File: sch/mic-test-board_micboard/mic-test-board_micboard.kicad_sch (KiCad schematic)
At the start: 25 parts, among them J1 Conn_01x01, J2 Conn_01x01, J3 Conn_01x01, J4 Conn_01x01, J5 Conn_01x01, J6 Conn_01x04, U1 ICS-40730, U2 THS4531AIRUNR

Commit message: pcb: finished routing mic board and ADC board.
 - BOM complete
 - uController pinout configured with CubeMX and re-checked
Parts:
- C6, C7: Manufacturer (none) -> Würth Elektronik; Part Number (none) -> 885012006027; Supplier (none) -> Digi-Key; Supplier Number (none) -> 732-7770-1-ND
- J1, J2, J3, J4, J5: now not fitted
- J6: value Conn_01x04 -> Conn_01x05; Manufacturer (none) -> Molex; Part Number (none) -> 0530470510; Supplier (none) -> Digi-Key; Supplier Number (none) -> WM1734-ND
- R1, R2: value 550R -> 549R; Manufacturer (none) -> YAGEO; Part Number (none) -> RC0603FR-07549RL; Supplier (none) -> Digi-Key; Supplier Number (none) -> 311-549HRCT-ND
- R3, R4: value 1.6k -> 1.58k; Manufacturer (none) -> YAGEO; Part Number (none) -> RC0603FR-071K58L; Supplier (none) -> Digi-Key; Supplier Number (none) -> 311-1.58KHRCT-ND
- U1: Manufacturer (none) -> TDK InvenSense; Part Number (none) -> ICS-40730; Supplier (none) -> Digi-Key; Supplier Number (none) -> 1428-1141-1-ND

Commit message: pcb: ordered PCB's and BOM! RevA and v240506
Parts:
- C1, C4: now in the parts list
- C11, C8: Manufacturer KEMET -> Samsung Electro-Mechanics; Part Number C0603C104K8RAC7867 -> CL10B105KP8NNNC; Supplier Number 399-C0603C104K8RAC7867CT-ND -> 1276-1946-1-ND
- J1, J2, J3, J4, J5: now fitted; now left out of the parts list
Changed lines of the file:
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@@
 		(unit 1)
 		(exclude_from_sim no)
-		(in_bom yes)
+		(in_bom no)
 		(on_board yes)
-		(dnp yes)
+		(dnp no)
 		(property "Reference" "J4"
 			(at 340.36 125.222 90)
@@
 	)
 	(symbol
+		(lib_name "THS4531AIRUNR_1")
 		(lib_id "mic-test-pcb:THS4531AIRUNR")
 		(at 231.14 146.05 0)
@@
 			)
 		)
-		(property "Description" "IC OPAMP DIFF 1 CIRCUIT 10WQFN"
+		(property "Description" "Ultralow Power, Low Distortion, Fully Differential ADC Drivers, Dual-Channel, "
 			(at 235.966 131.318 0)
 			(effects
@@
 		)
 		(pin "1"
+		)
+		(pin "8"
+		)
+		(pin "2"
 		)
 		(instances
@@
 			)
 		)
-		(property "Description" "IC OPAMP DIFF 1 CIRCUIT 10WQFN"
+		(property "Description" "Ultralow Power, Low Distortion, Fully Differential ADC Drivers, Dual-Channel, "
 			(at 221.996 227.838 0)
 			(effects
@@
 		(unit 1)
 		(exclude_from_sim no)
-		(in_bom yes)
+		(in_bom no)
 		(on_board yes)
-		(dnp yes)
+		(dnp no)
 		(property "Reference" "J2"
 			(at 332.74 125.222 90)
@@
 		(unit 1)
 		(exclude_from_sim no)
-		(in_bom yes)
+		(in_bom no)
 		(on_board yes)
-		(dnp yes)
+		(dnp no)
 		(property "Reference" "J1"
 			(at 328.93 125.222 90)
@@
 			)
 		)
-		(property "Manufacturer" "KEMET"
+		(property "Manufacturer" "Samsung Electro-Mechanics"
 			(at 254 243.84 0)
 			(effects
@@
 			)
 		)
-		(property "Part Number" "C0603C104K8RAC7867"
+		(property "Part Number" "CL10B105KP8NNNC"
 			(at 254 243.84 0)
 			(effects
@@
 			)
 		)
-		(property "Supplier Number" "399-C0603C104K8RAC7867CT-ND"
+		(property "Supplier Number" "1276-1946-1-ND"
 			(at 254 243.84 0)
 			(effects
@@
 		(unit 1)
 		(exclude_from_sim no)
-		(in_bom yes)
+		(in_bom no)
 		(on_board yes)
-		(dnp yes)
+		(dnp no)
 		(property "Reference" "J5"
 			(at 344.17 125.222 90)
@@
 		(unit 1)
 		(exclude_from_sim no)
-		(in_bom no)
+		(in_bom yes)
 		(on_board yes)
 		(dnp yes)
@@
 			)
 		)
-		(property "Manufacturer" "KEMET"
+		(property "Manufacturer" "Samsung Electro-Mechanics"
 			(at 194.31 242.57 0)
 			(effects
@@
 			)
 		)
-		(property "Part Number" "C0603C104K8RAC7867"
+		(property "Part Number" "CL10B105KP8NNNC"
 			(at 194.31 242.57 0)
 			(effects
@@
 			)
 		)
-		(property "Supplier Number" "399-C0603C104K8RAC7867CT-ND"
+		(property "Supplier Number" "1276-1946-1-ND"
 			(at 194.31 242.57 0)
 			(effects
@@
 		(unit 1)
 		(exclude_from_sim no)
-		(in_bom no)
+		(in_bom yes)
 		(on_board yes)
 		(dnp yes)
@@
 		(unit 1)
 		(exclude_from_sim no)
-		(in_bom yes)
+		(in_bom no)
 		(on_board yes)
-		(dnp yes)
+		(dnp no)
 		(property "Reference" "J3"
 			(at 336.55 125.222 90)

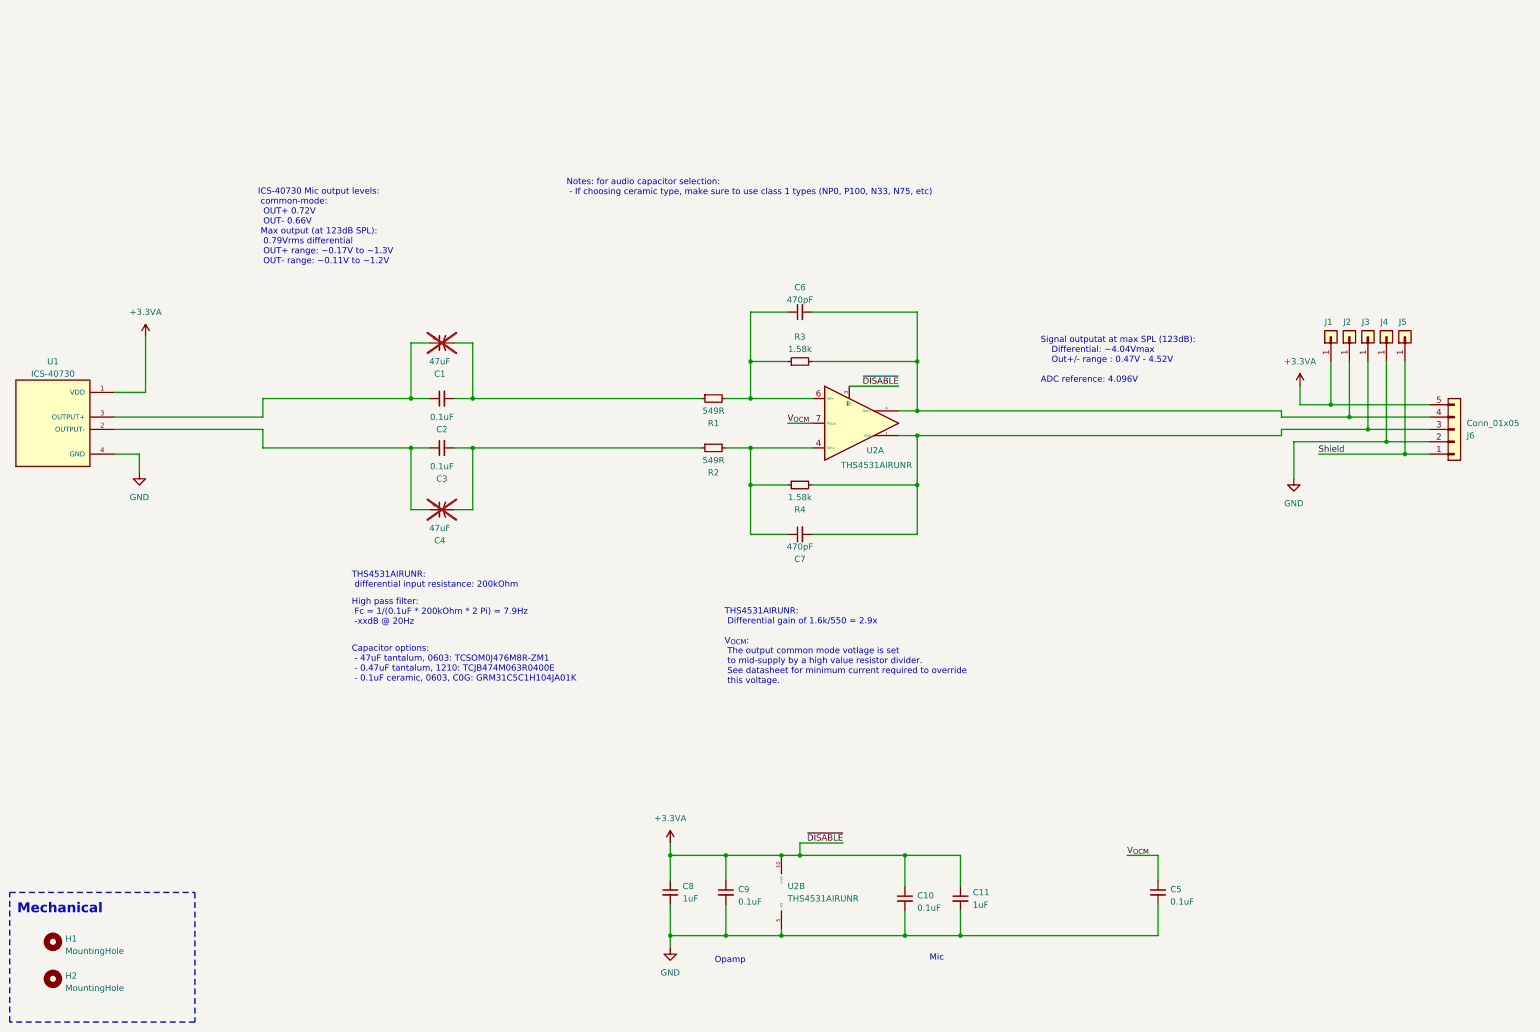
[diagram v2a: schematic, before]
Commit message: sch: adding bringup notes
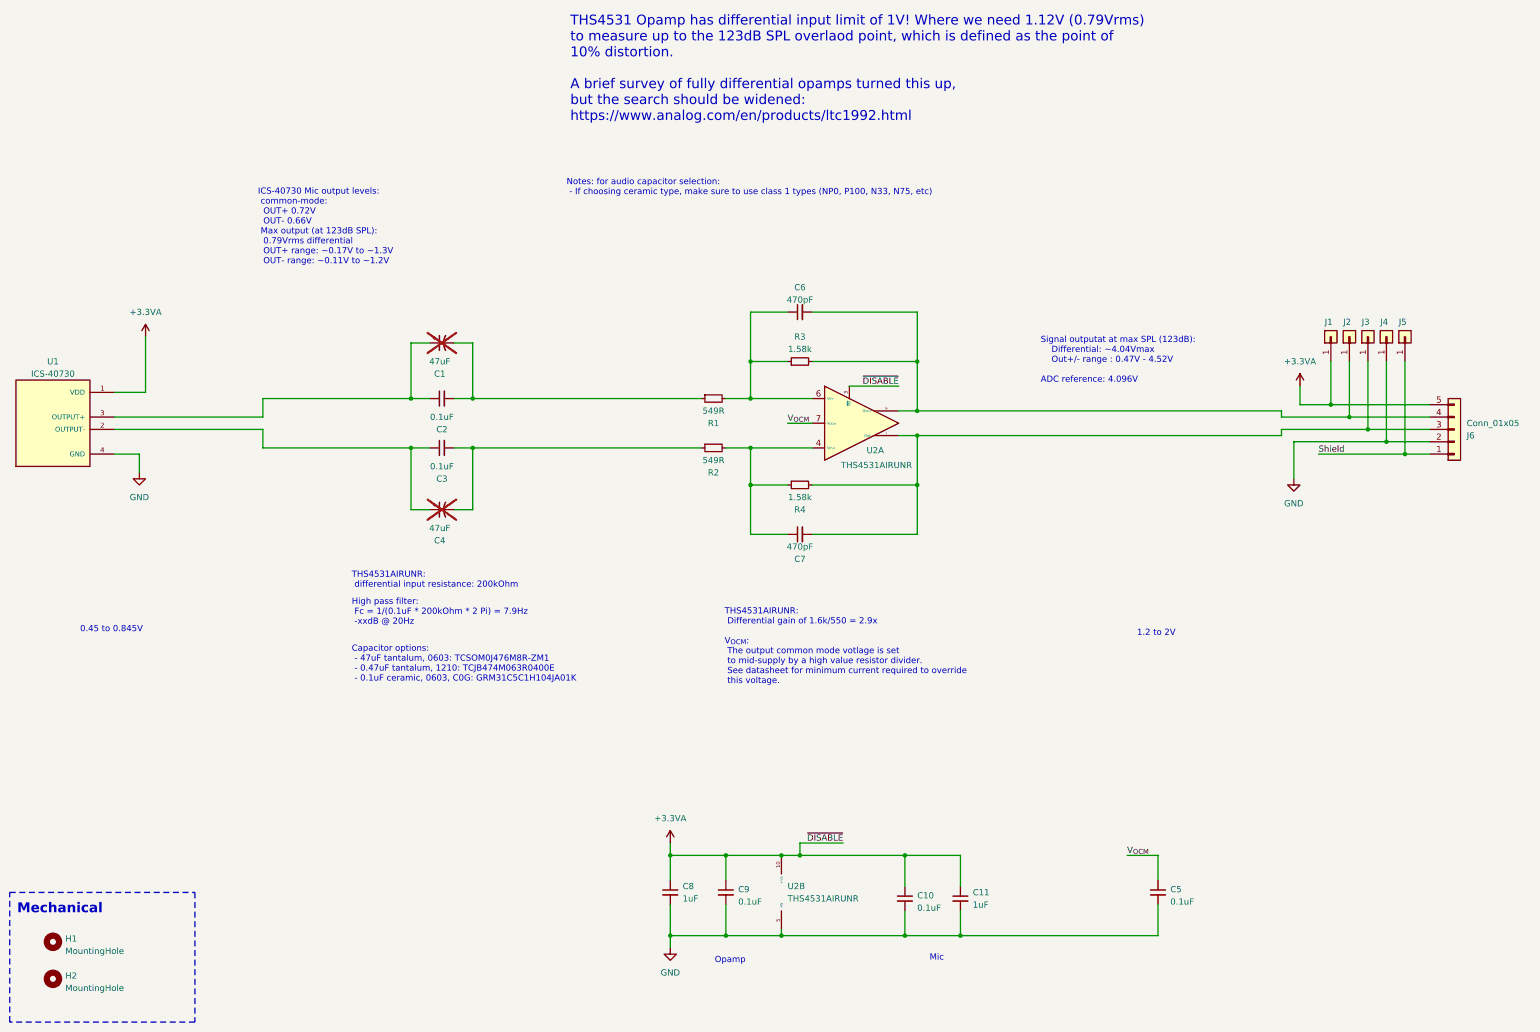
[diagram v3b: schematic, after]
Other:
- note added: "0.45 to 0.845V"
- note added: "1.2 to 2V"
- note added: "THS4531 Opamp has differential input limit of 1V! Where we need 1.12V (0.79Vrms) to measure up to the 123dB SPL overlaod point, which is defined as the point of 10% distortion. A brief survey of fully differential opamps turned this up, but the search should be widened: https://www.analog.com/en/products/ltc1992.html"
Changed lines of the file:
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@@
+		)
+	)
+	(text "THS4531 Opamp has differential input limit of 1V! Where we need 1.12V (0.79Vrms) \nto measure up to the 123dB SPL overlaod point, which is defined as the point of \n10% distortion. \n\nA brief survey of fully differential opamps turned this up, \nbut the search should be widened:\nhttps://www.analog.com/en/products/ltc1992.html"
+		(exclude_from_sim no)
+		(at 173.736 73.152 0)
+		(effects
+			(font
+				(size 2.032 2.032)
+			)
+			(justify left)
 		)
 	)
@@
 		(exclude_from_sim no)
 		(at 128.778 180.086 0)
+		(effects
+			(font
+				(size 1.27 1.27)
+			)
+			(justify left bottom)
+		)
+	)
+	(text "0.45 to 0.845V"
+		(exclude_from_sim no)
+		(at 72.898 189.23 0)
 		(effects
 			(font
@@
 		(effects
 			(font
+				(size 1.27 1.27)
+			)
+			(justify left bottom)
+		)
+	)
+	(text "1.2 to 2V\n"
+		(exclude_from_sim no)
+		(at 290.322 189.992 0)
+		(effects
+			(font
